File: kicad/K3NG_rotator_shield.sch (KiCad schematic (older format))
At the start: 19 parts, among them P1 Power, P2 Analog, P3 Digital, P4 Digital, P5 CONN_01X01, P6 CONN_01X01, P7 CONN_01X01, P8 CONN_01X01

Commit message: Ready for final proofread
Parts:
- removed C?: 10u, symbol Device:C
- added C4: 10u, Capacitor_THT:CP_Radial_D4.0mm_P2.00mm, symbol Device:CP
- added SW1: SW_Push_Dual, Button_Switch_THT:SW_PUSH_6mm_H4.3mm, symbol Switch:SW_Push_Dual
- C1, C2, C3: renamed from C?; footprint (none) -> Capacitor_THT:C_Disc_D4.3mm_W1.9mm_P5.00mm
- J1: renamed from J?; footprint (none) -> SamacSys_Parts:1725698
- Q1, Q2: renamed from Q?; footprint JANTX2N2222A -> SamacSys_Parts:JANTX2N2222A
- R1, R2, R3, R4: renamed from R?; footprint (none) -> Resistor_THT:R_Axial_DIN0204_L3.6mm_D1.6mm_P5.08mm_Horizontal
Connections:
- wire segments 61 -> 73
- no-connect marks 5 -> 23

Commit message: Part selection and layout complete
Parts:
- removed C1, C2, C3: .01u, Capacitor_THT:C_Disc_D4.3mm_W1.9mm_P5.00mm, symbol Device:C
- removed C4: 10u, Capacitor_THT:CP_Radial_D4.0mm_P2.00mm, symbol Device:CP
- removed P5, P6, P7, P8: CONN_01X01, Socket_Arduino_Uno:Arduino_1pin, symbol Connector_Generic:Conn_01x01
- removed Q1, Q2: 2N2222Ae3, SamacSys_Parts:JANTX2N2222A, symbol SamacSys_Parts:2N2222Ae3
- removed R1, R2, R4: 1k, Resistor_THT:R_Axial_DIN0204_L3.6mm_D1.6mm_P5.08mm_Horizontal, symbol Device:R
- removed R3: 4k7, Resistor_THT:R_Axial_DIN0204_L3.6mm_D1.6mm_P5.08mm_Horizontal, symbol Device:R
- removed SW1: SW_Push_Dual, Button_Switch_THT:SW_PUSH_6mm_H4.3mm, symbol Switch:SW_Push_Dual
- added C1, C2, C3: RDER71H103K0M1H03A, SamacSys_Parts:RCE5C1H103J1A2H03B, symbol SamacSys_Parts:RDER71H103K0M1H03A
- added C4: EEA-GA1E100B, SamacSys_Parts:CAPPRD150W50D400H800, symbol SamacSys_Parts:EEA-GA1E100B
- added Q1, Q2: 2N2222A, SamacSys_Parts:TO-18_4, symbol SamacSys_Parts:2N2222A
- added R1, R2, R4: CFM14JT1K00, CFM14JT1K0:CFM14JT1K00, symbol 2021-02-19_01-51-00:CFM14JT1K00
- added R3: CFM14JT4K70, CFM14JT4K70:CFM14JT4K70, symbol 2021-02-19_01-40-20:CFM14JT4K70
- added S1: D6C40F2LFS, SamacSys_Parts:D6C40F2LFS, symbol SamacSys_Parts:D6C40F2LFS
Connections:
- net 6(**): now also R4.2
- net 7: now also R2.2
- net 8: now also R3.2
- net A0: now also R1.1
- net A4(SDA): no longer P2.5 (Pin_5), P3.2 (Pin_2)
- net A5(SCL): no longer P2.6 (Pin_6), P3.1 (Pin_1)
- net AZctlr: now also C1.1, R1.2
- net CCWctlr: now also C2.2, Q1.3
- net CWctlr: now also C3.1, Q2.3
- net GND: now also C1.2, C2.1, C3.2, C4.1, Q1.2, Q2.2, S1.1 (COM_1), S1.2 (COM_2)
- net Reset: now also S1.3 (NO_1), S1.4 (NO_2)
- net SPDctlr: now also C4.2, R3.1
- new net: Q2.1, R4.1
- new net: Q1.1, R2.1
- no-connect marks 23 -> 27
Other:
- note removed: "Holes"

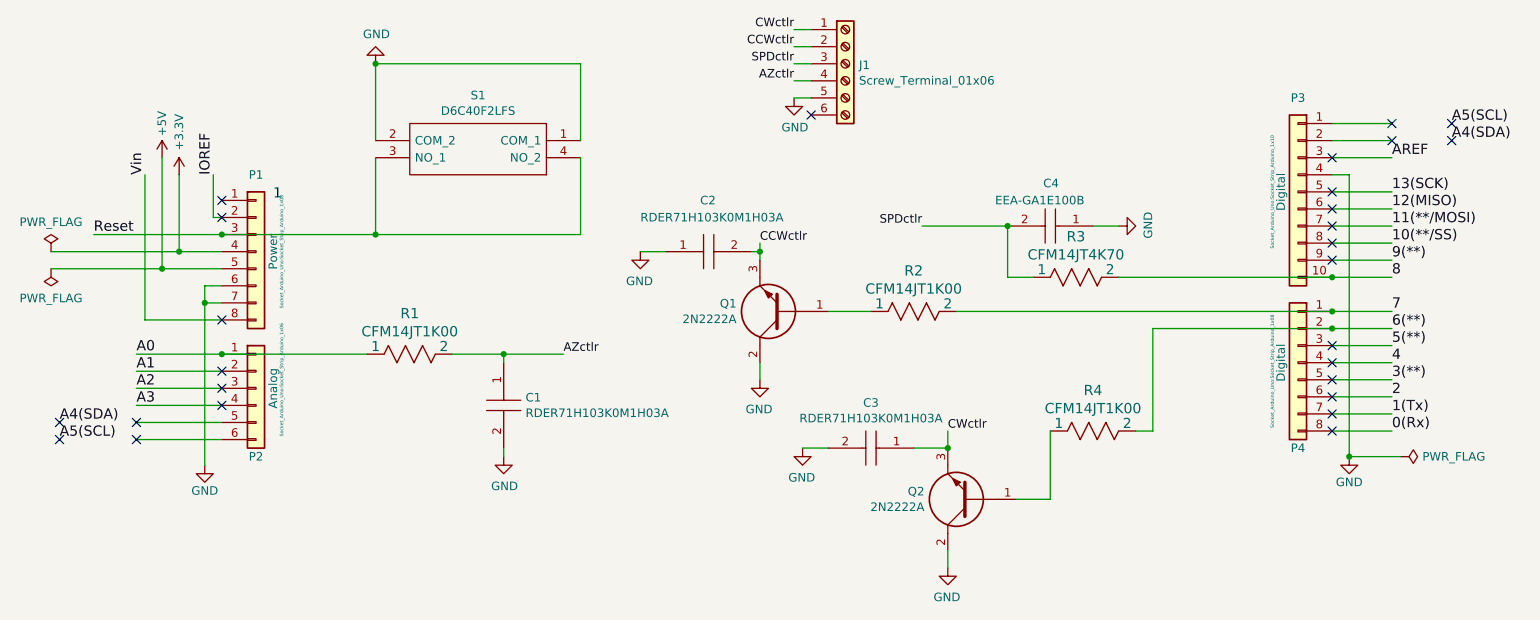
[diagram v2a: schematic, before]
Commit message: Fixed mistakes, generated Gerbers, ordered
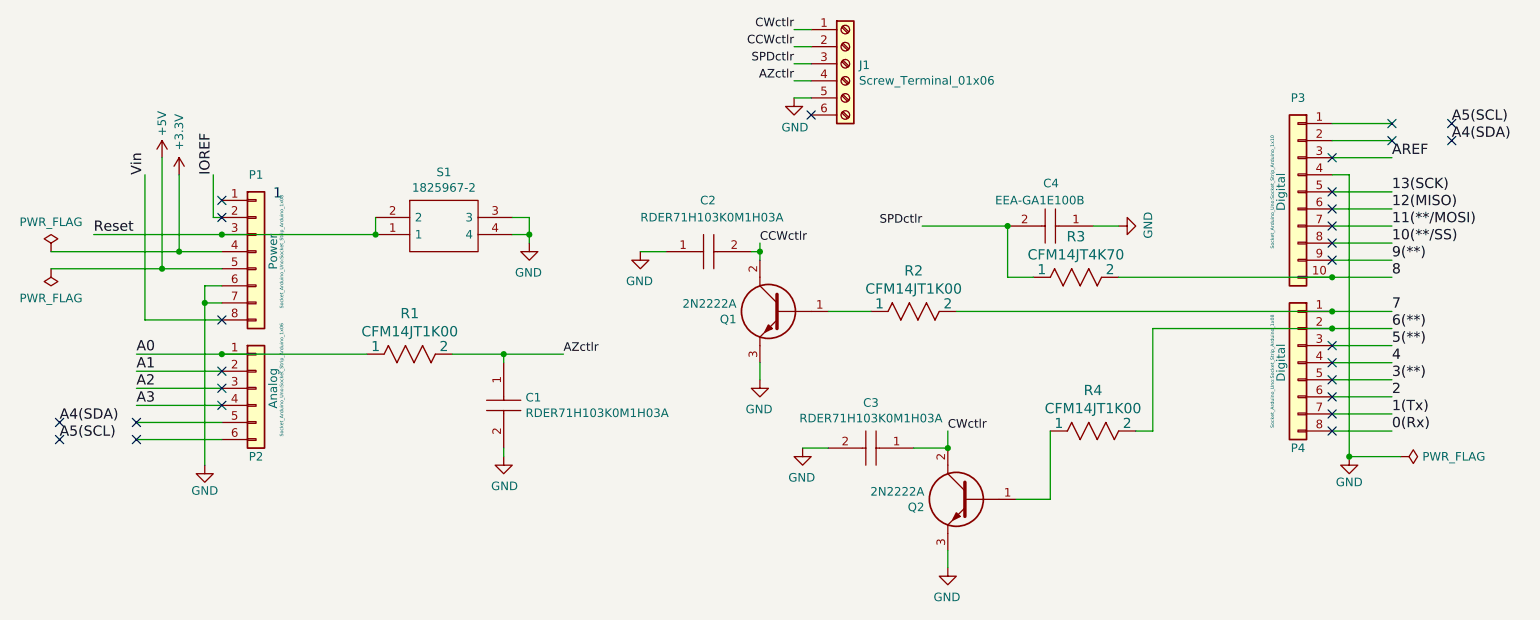
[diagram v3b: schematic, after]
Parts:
- removed S1: D6C40F2LFS, SamacSys_Parts:D6C40F2LFS, symbol SamacSys_Parts:D6C40F2LFS
- added S1: 1825967-2, SamacSys_Parts:18259672, symbol SamacSys_Parts:1825967-2
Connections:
- net CCWctlr: now also Q1.2; no longer Q1.3
- net CWctlr: now also Q2.2; no longer Q2.3
- net GND: now also Q1.3, Q2.3, S1.3, S1.4; no longer Q1.2, Q2.2
- net Reset: now also S1.1, S1.2
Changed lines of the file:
@@
 L power:GND #PWR011
 U 1 1 602D6E17
-P 3150 2250
-F 0 "#PWR011" H 3150 2000 50  0001 C CNN
-F 1 "GND" H 3155 2077 50  0000 C CNN
-F 2 "" H 3150 2250 50  0001 C CNN
-F 3 "" H 3150 2250 50  0001 C CNN
-	1    3150 2250
-	1    0    0    1
+P 4050 3300
+F 0 "#PWR011" H 4050 3050 50  0001 C CNN
+F 1 "GND" H 4055 3127 50  0000 C CNN
+F 2 "" H 4050 3300 50  0001 C CNN
+F 3 "" H 4050 3300 50  0001 C CNN
+	1    4050 3300
+	-1   0    0    -1
 $EndComp
 Wire Wire Line
@@
 F 11 "" H 7450 3750 50  0001 L CNN "Arrow Price/Stock"
 	1    6900 4800
-	-1   0    0    1
+	-1   0    0    -1
 $EndComp
 Connection ~ 6500 4500
@@
 F 11 "" H 6350 2650 50  0001 L CNN "Arrow Price/Stock"
 	1    5800 3700
-	-1   0    0    1
+	-1   0    0    -1
 $EndComp
 Wire Wire Line
 	7100 4400 7100 4800
-$Comp
-L SamacSys_Parts:D6C40F2LFS S1
-U 1 1 60389B07
-P 4350 2800
-F 0 "S1" H 4950 2435 50  0000 C CNN
-F 1 "D6C40F2LFS" H 4950 2526 50  0000 C CNN
-F 2 "SamacSys_Parts:D6C40F2LFS" H 5400 2900 50  0001 L CNN
-F 3 "https://www.arrow.com/en/products/d6c40f2lfs/ck" H 5400 2800 50  0001 L CNN
-F 4 "Pushbutton Switches Key Switch N.O. SPDT 100 mA" H 5400 2700 50  0001 L CNN "Description"
-F 5 "9.8" H 5400 2600 50  0001 L CNN "Height"
-F 6 "C & K COMPONENTS" H 5400 2500 50  0001 L CNN "Manufacturer_Name"
-F 7 "D6C40F2LFS" H 5400 2400 50  0001 L CNN "Manufacturer_Part_Number"
-F 8 "611-D6C40F2LFS" H 5400 2300 50  0001 L CNN "Mouser Part Number"
-F 9 "https://www.mouser.co.uk/ProductDetail/CK/D6C40F2LFS/?qs=sb%252But3Lm4x0zytIpqAQYSQ%3D%3D" H 5400 2200 50  0001 L CNN "Mouser Price/Stock"
-F 10 "D6C40F2LFS" H 5400 2100 50  0001 L CNN "Arrow Part Number"
-F 11 "https://www.arrow.com/en/products/d6c40f2lfs/ck" H 5400 2000 50  0001 L CNN "Arrow Price/Stock"
-	1    4350 2800
-	-1   0    0    1
-$EndComp
-Wire Wire Line
-	3150 3250 3150 2800
-Wire Wire Line
-	3150 3250 4350 3250
-Wire Wire Line
-	4350 3250 4350 2800
-Connection ~ 3150 3250
-Wire Wire Line
-	3150 2700 3150 2250
-Wire Wire Line
-	4350 2700 4350 2250
-Wire Wire Line
-	4350 2250 3150 2250
-Connection ~ 3150 2250
 NoConn ~ 1300 4450
 NoConn ~ 1300 4350
@@
 Wire Wire Line
 	6550 3700 8750 3700
+$Comp
+L SamacSys_Parts:1825967-2 S1
+U 1 1 6030171D
+P 3150 3150
+F 0 "S1" H 3550 3415 50  0000 C CNN
+F 1 "1825967-2" H 3550 3324 50  0000 C CNN
+F 2 "SamacSys_Parts:18259672" H 3800 3250 50  0001 L CNN
+F 3 "http://www.farnell.com/cad/1885104.pdf?_ga=2.168058273.1018450153.1518464186-2047430813.1516449236" H 3800 3150 50  0001 L CNN
+F 4 "Tactile switch,PCB,SPST,high temp,sq act" H 3800 3050 50  0001 L CNN "Description"
+F 5 "7" H 3800 2950 50  0001 L CNN "Height"
+F 6 "TE Connectivity" H 3800 2850 50  0001 L CNN "Manufacturer_Name"
+F 7 "1825967-2" H 3800 2750 50  0001 L CNN "Manufacturer_Part_Number"
+F 8 "N/A" H 3800 2650 50  0001 L CNN "Mouser Part Number"
+F 9 "https://www.mouser.co.uk/ProductDetail/TE-Connectivity/1825967-2/?qs=bdENzIhz2rnlrAt6CULBDw%3D%3D" H 3800 2550 50  0001 L CNN "Mouser Price/Stock"
+F 10 "1825967-2" H 3800 2450 50  0001 L CNN "Arrow Part Number"
+F 11 "https://www.arrow.com/en/products/1825967-2/te-connectivity" H 3800 2350 50  0001 L CNN "Arrow Price/Stock"
+	1    3150 3150
+	1    0    0    -1
+$EndComp
+Wire Wire Line
+	3150 3150 3150 3250
+Connection ~ 3150 3250
+Wire Wire Line
+	3950 3150 4050 3150
+Wire Wire Line
+	3950 3250 4050 3250
+Wire Wire Line
+	4050 3250 4050 3150
+Wire Wire Line
+	4050 3300 4050 3250
+Connection ~ 4050 3250
 $EndSCHEMATC
